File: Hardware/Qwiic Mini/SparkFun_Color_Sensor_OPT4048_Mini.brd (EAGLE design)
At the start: 25.4 x 12.7 mm, 34 parts, among them J4 QWIIC_RIGHT_ANGLE, J5 QWIIC_RIGHT_ANGLE

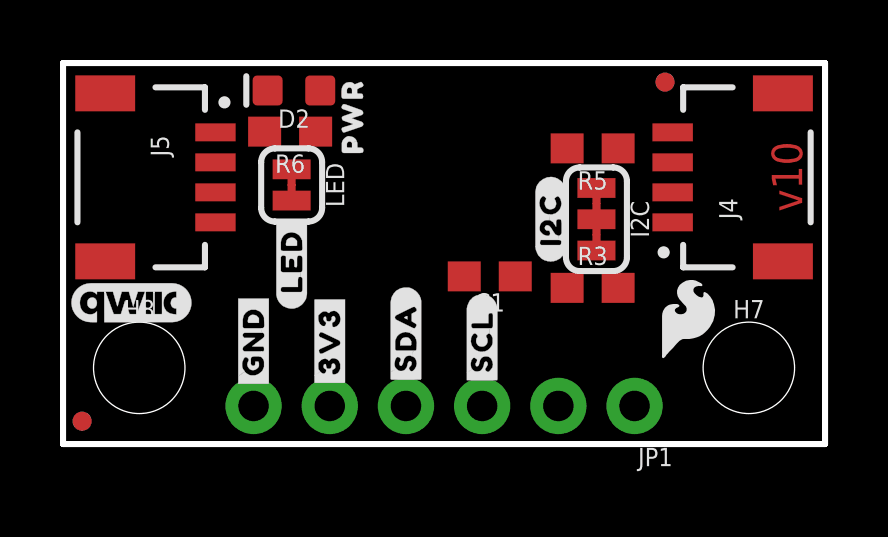
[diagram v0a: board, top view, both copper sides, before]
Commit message: Finishes routing Qwiic mini
* Adds silk to Qwiic mini
* Adds ordering instructions
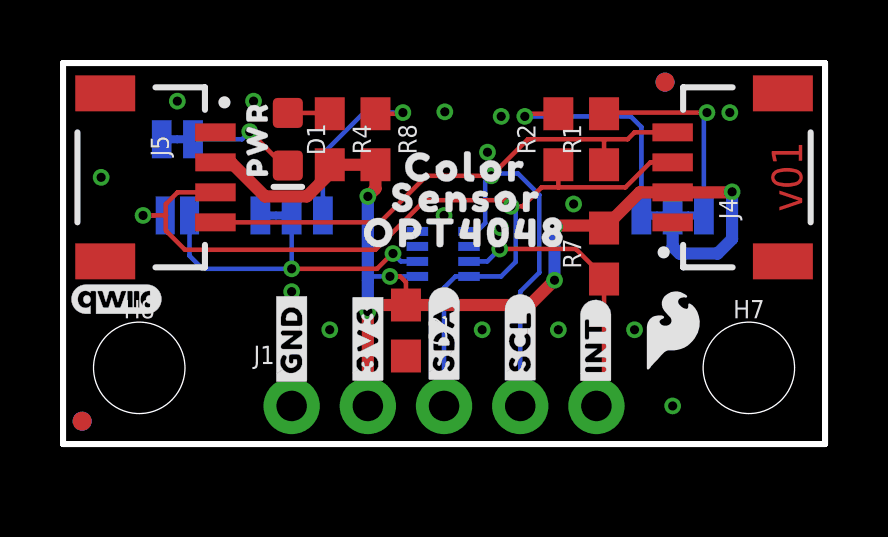
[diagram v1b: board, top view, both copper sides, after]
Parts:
- removed C1: 0.1uF, SparkFun-Capacitors:0603
- removed D2: RED, SparkFun-LED:LED-0603
- removed I2C: I2C_PU, SparkFun-Jumpers:SMT-JUMPER_3_2-NC_TRACE_SILK
- removed JP1: IO, SparkFun-Connectors:1X06_NO_SILK
- removed R3, R5: 2.2k, SparkFun-Resistors:0603
- removed R6: 4.7k, SparkFun-Resistors:0603
- removed U$18: (no value), TMFHQBotSilk:#SDA#6
- added ADDR: JUMPER-SMT_3_1-NC_TRACE_SILK, SparkFun-Jumpers:SMT-JUMPER_3_1-NC_TRACE_SILK
- added ADDR2: JUMPER-SMT_2_NO_SILK, SparkFun-Jumpers:SMT-JUMPER_2_NO_SILK
- added C2: 0.1uF, SparkFun-Capacitors:0603
- added D1: RED, SparkFun-LED:LED-0603
- added I2C_PU: S_MODE, SparkFun-Jumpers:SMT-JUMPER_3_2-NC_TRACE_SILK
- added J1: (no value), SparkFun-Connectors:1X05_NO_SILK
- added LOGO4: SPECIAL_INSTRUCTIONS-ORDERING, SparkFun-Aesthetics:ORDERING_INSTRUCTIONS
- added R1, R2: 2.2k, SparkFun-Resistors:0603
- added R4: 1k, SparkFun-Resistors:0603
- added R7, R8: 10k, SparkFun-Resistors:0603
- added U$1: (no value), top_small:#INT#9
- added U$11: (no value), bot_small:SENSOR15
- added U$2: (no value), top_small:COLOR_SENSOR227
- added U$3: (no value), top_small:OPT4048229
- added U$4: (no value), bot_small:#LED#12
- added U$5: (no value), bot_small:#ADDR#11
- added U$6: (no value), bot_small:#ADDR2#12
- added U$7: (no value), bot_small:#INT#3
- added U$8: (no value), SparkFun-Aesthetics:SFE_LOGO_NAME_.1
- added U$9: (no value), bot_small:COLOR14
- added U1: OPT4048, Color_Sensor:FCSOT
- LED: value LED -> JUMPER-SMT_2_NC_TRACE_SILK
- LOGO2: value QWIIC_LOGO_4MM -> QWIIC_LOGO_3MM; device SparkFun-Aesthetics:QWIIC_4MM -> SparkFun-Aesthetics:QWIIC_3MM
- U$12: device SparkFun-Aesthetics:SFE_LOGO_FLAME_.2 -> top_small:OPT4048229
- U$13: device TMFMiniBotSilk:#LED#10 -> bot_small:#SDA#1
- moved U$15 18.0 mm to (20.3, 3.94)
- moved U$12 11.0 mm to (13.4, 7.04), flipped to the top
- moved U$13 5.69 mm to (12.7, 3.53), flipped to the bottom, turned to 270 degrees
- moved FRAME2 4.58 mm to (-14.5, -16.8)
- moved LOGO1 4.58 mm to (-14.5, -16.8)
- moved LOGO3 4.58 mm to (-14.5, -16.8)
- moved U$20 4.30 mm to (20.3, 6.10), flipped to the bottom, turned to 0 degrees
- moved LED 4.10 mm to (3.81, 10.2), flipped to the bottom, turned to 180 degrees
- moved U$43 3.27 mm to (6.48, 10.2)
- moved U$16 1.27 mm to (7.62, 3.51)
- moved U$38 1.27 mm to (7.62, 3.51)
- moved U$10 1.27 mm to (10.2, 3.51)
- moved U$37 1.27 mm to (10.2, 3.51)
- moved U$19 1.27 mm to (15.2, 3.43)
- moved U$39 1.27 mm to (15.2, 3.43)
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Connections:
- removed net N$5: D2.A, R6.1
- removed net N$6: LED.1, R6.2
- removed net N$7: I2C.3, R3.2
- removed net N$8: I2C.1, R5.2
- new net N$1: I2C_PU.1, R1.2
- new net N$2: I2C_PU.3, R2.2
- new net N$3: D1.A, R4.1
- new net N$4: D1.C, LED.2
- new net N$9: ADDR.1, R8.1
- net 3.3V: now also C2.1, I2C_PU.2, J1.2, R4.2, R7.2, R8.2, U1.P1; no longer C1.1, I2C.2, JP1.5, LED.2
- net ADDR: now also ADDR.2, ADDR2.1, U1.P2; no longer JP1.1
- net GND: now also ADDR.3, C2.2, J1.1, LED.1, U1.P4; no longer C1.2, D2.C, JP1.6
- net INT: now also J1.5, R7.1, U1.P7; no longer JP1.2
- net SCL: now also J1.4, R1.1, U1.P5; no longer JP1.3, R5.1
- net SDA: now also ADDR2.2, J1.3, R2.1, U1.P8; no longer JP1.4, R3.1
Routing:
- net 3.3V: track 0.00 -> 37.5 mm, vias 0 -> 6
- net SDA: track 0.00 -> 32.1 mm, vias 0 -> 2
- net SCL: track 0.00 -> 28.9 mm, vias 0 -> 1
- net ADDR: track 0.00 -> 11.2 mm, vias 0 -> 2
- net INT: track 0.00 -> 9.46 mm, vias 0 -> 1
- net N$2: track 0.00 -> 8.13 mm, vias 0 -> 1
- net N$1: track 0.00 -> 6.92 mm, vias 0 -> 1
- net N$9: track 0.00 -> 6.22 mm, vias 0 -> 1
- net N$4: track 0.00 -> 3.74 mm, vias 0 -> 1
- net N$3: track 0.00 -> 1.41 mm
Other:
- board text added: "1.6mm Thickness 1 oz. Copper Lead-Free HASL finish Material: TG135-140 Red Soldermask White Silkscreen"
- board text added: "v01"
- board text removed: "v10"

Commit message: Changes address selection on the mini
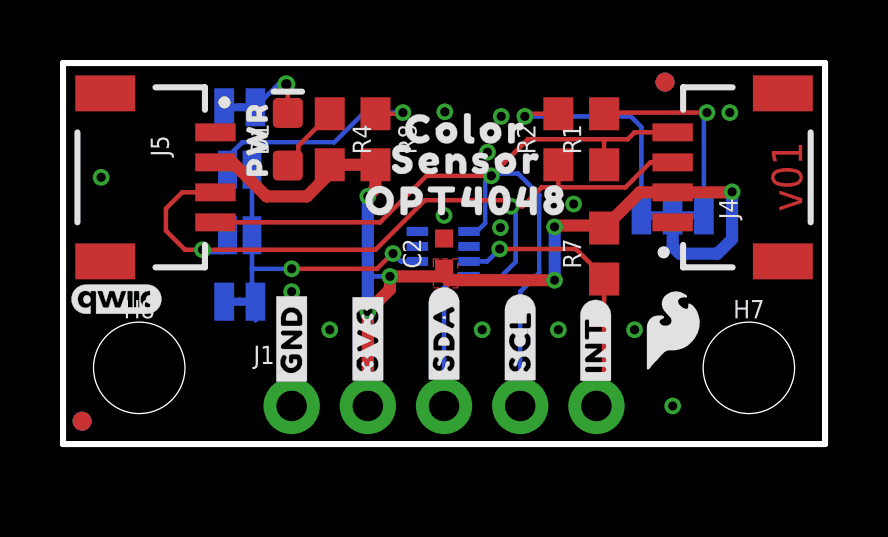
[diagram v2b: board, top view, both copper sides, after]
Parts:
- removed ADDR: JUMPER-SMT_3_1-NC_TRACE_SILK, SparkFun-Jumpers:SMT-JUMPER_3_1-NC_TRACE_SILK
- removed ADDR2: JUMPER-SMT_2_NO_SILK, SparkFun-Jumpers:SMT-JUMPER_2_NO_SILK
- added 0X44: JUMPER-SMT_2_NC_TRACE_SILK, SparkFun-Jumpers:SMT-JUMPER_2_NC_TRACE_SILK
- added 0X45, 0X46: JUMPER-SMT_2_NO_SILK, SparkFun-Jumpers:SMT-JUMPER_2_NO_SILK
- added U$14: (no value), bot_small:#LED#11
- C2: device SparkFun-Capacitors:0603 -> SparkFun-Capacitors:0402-TIGHT
- U$4: device bot_small:#LED#12 -> bot_small:#0X44#11
- U$5: device bot_small:#ADDR#11 -> bot_small:#0X46#11
- U$6: device bot_small:#ADDR2#12 -> bot_small:#0X45#11
- moved U$4 5.94 mm to (3.07, 4.75)
- moved U$5 4.40 mm to (3.23, 6.96)
- moved U$6 2.99 mm to (3.25, 9.09)
- moved C2 2.86 mm to (12.7, 6.35), turned to 90 degrees
- moved LED 2.34 mm to (5.89, 11.2)
- moved U$11 1.27 mm to (13.5, 9.47)
- moved U$9 1.27 mm to (13.4, 10.5)
- moved U$12 1.07 mm to (13.5, 8.10)
- moved U$16 0.13 mm to (7.75, 3.48)
- turned D1 to 90 degrees
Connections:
- net ADDR: now also 0X44.1, 0X45.1, 0X46.1; no longer ADDR.2, ADDR2.1
- net GND: now also 0X44.2; no longer ADDR.3
- net N$9: now also 0X45.2; no longer ADDR.1
- net SDA: now also 0X46.2; no longer ADDR2.2
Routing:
- net N$9: track 6.22 -> 7.81 mm
- net N$4: track 3.74 -> 2.32 mm
- net 3.3V: track 37.5 -> 36.5 mm
- net N$3: track 1.41 -> 2.31 mm
- added copper zone on layer 1, net 3.3V
